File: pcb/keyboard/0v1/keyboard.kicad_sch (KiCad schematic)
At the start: 1 part, among them U1 113990583

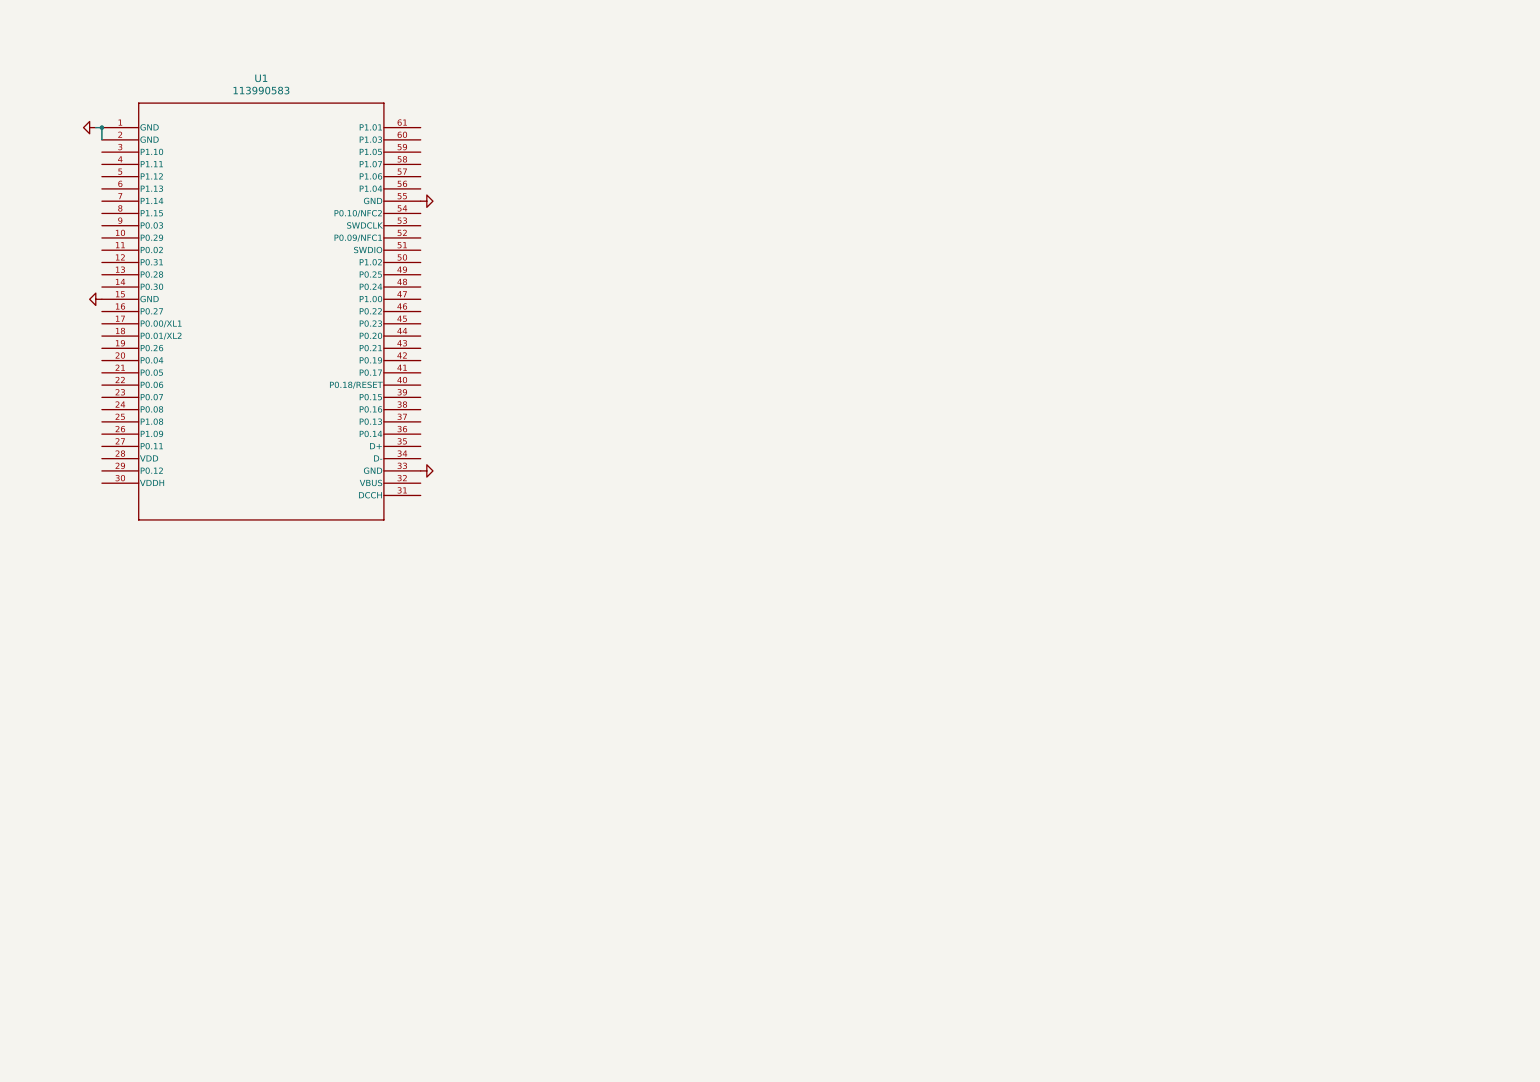
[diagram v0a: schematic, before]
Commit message: Basic power management circuit for the nrf52840 module.
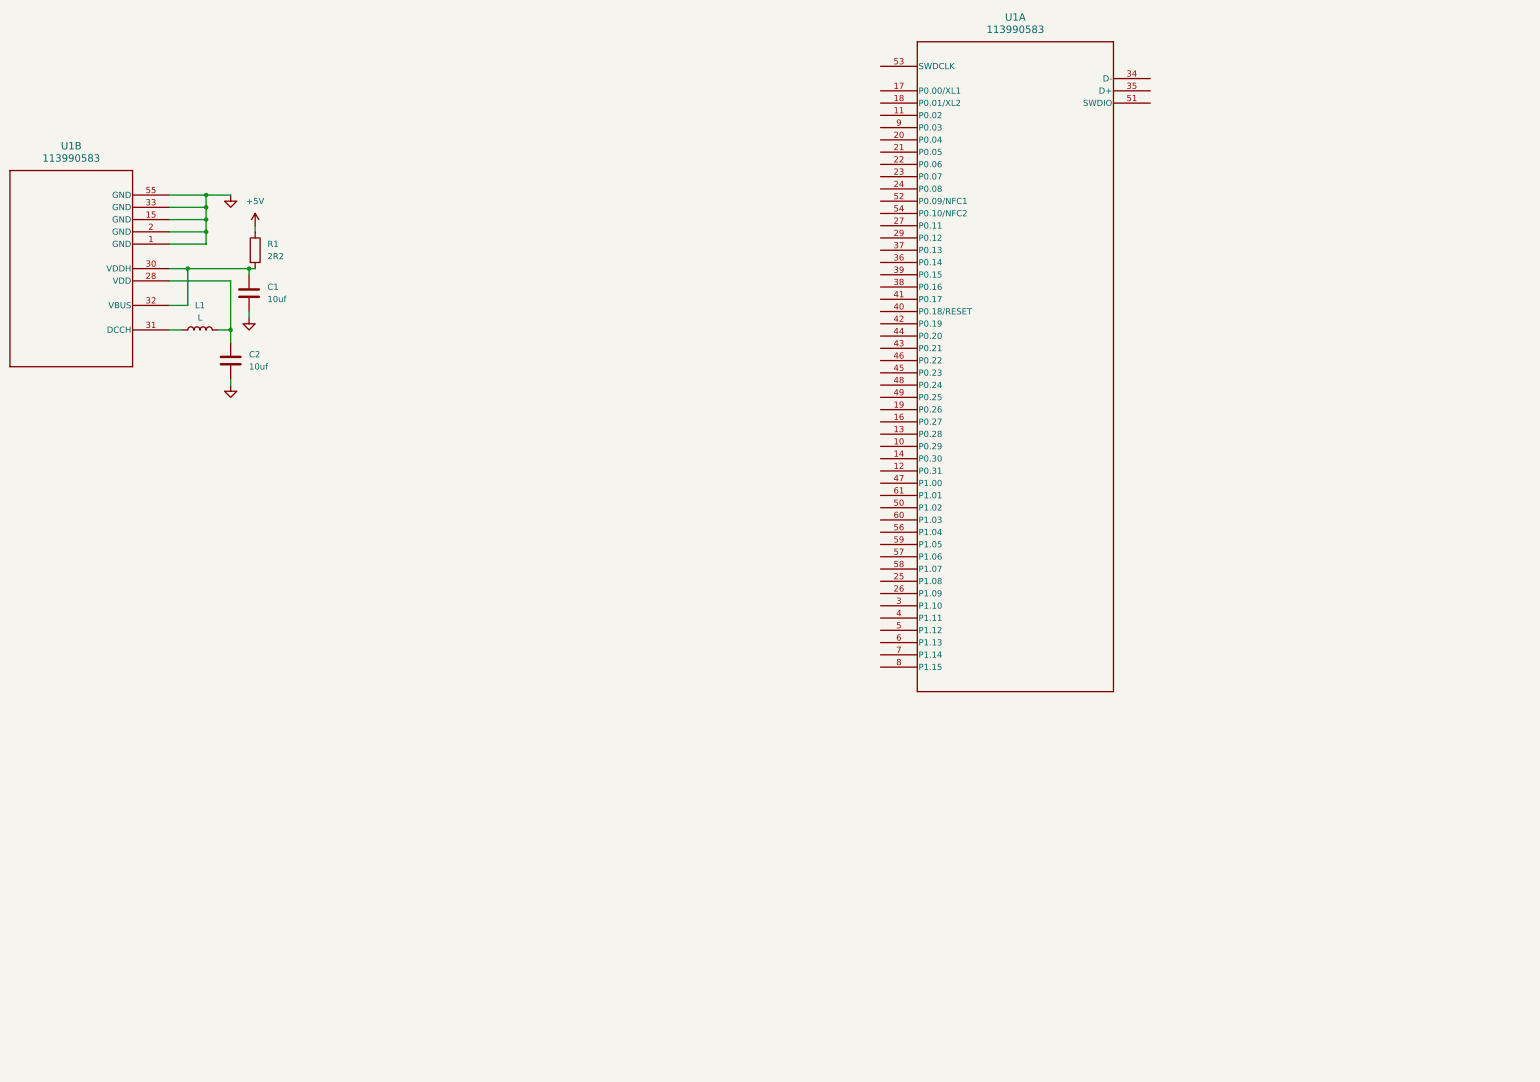
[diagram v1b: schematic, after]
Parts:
- added C1, C2: 10uf, Capacitor_SMD:C_0805_2012Metric, symbol Device:C
- added L1: L, Inductor_SMD:L_0603_1608Metric, symbol Device:L
- added R1: 2R2, Resistor_SMD:R_0603_1608Metric, symbol Device:R
- added unit 2 of U1
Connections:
- net GND: now also C1.2, C2.2, U1.1 (GND), U1.15 (GND), U1.2 (GND), U1.33 (GND), U1.55 (GND); no longer U1.1 (GND), U1.15 (GND), U1.2 (GND), U1.33 (GND), U1.55 (GND)
- new net: C2.1, L1.2, U1.28 (VDD)
- new net: C1.1, R1.2, U1.30 (VDDH), U1.32 (VBUS)
- new net: L1.1, U1.31 (DCCH)
- new net +5V: R1.1
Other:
- company: (none) -> Teahaz
- title: (none) -> TH-A10C keyboard

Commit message: Add USB and SWD Pogo connectors.
These are custom symbols, the footprint for them is yet to be added.
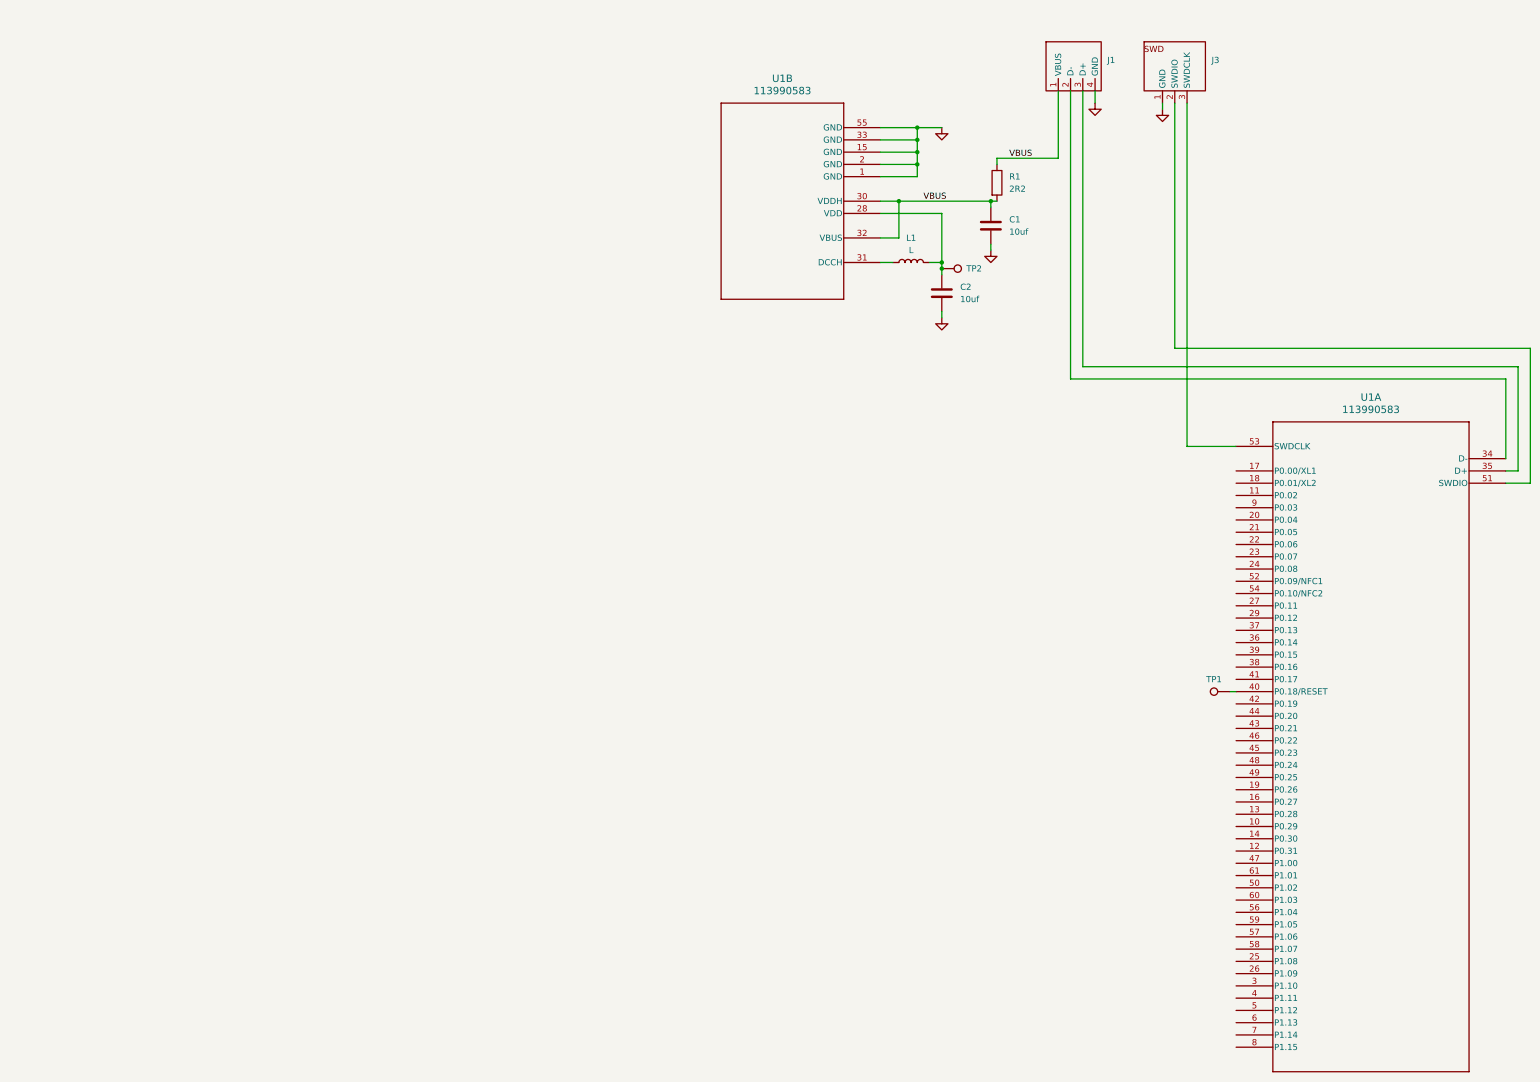
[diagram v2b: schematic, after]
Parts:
- added J1: ~, symbol TH-A10C:USB2_POGO_4
- added J3: ~, symbol TH-A10C:SWD_POGO_3
- added TP1, TP2: TestPoint, TestPoint:TestPoint_Pad_D2.0mm, symbol Connector:TestPoint
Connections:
- net +5V is gone; now on net VBUS: R1.1
- net GND: now also J1.4 (GND), J3.1 (GND)
- net at C2.1, L1.2, U1.28 (VDD): now also TP2.1
- net VBUS: now reaches C1.1, R1.2, U1.30 (VDDH), U1.32 (VBUS)
- net VBUS: now also J1.1 (VBUS)
- net at U1.34 (D-): now also J1.2 (D-)
- net at U1.35 (D+): now also J1.3 (D+)
- net at U1.40 (P0.18/RESET): now also TP1.1
- net at U1.51 (SWDIO): now also J3.2 (SWDIO)
- net at U1.53 (SWDCLK): now also J3.3 (SWDCLK)
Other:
- moved on the sheet: C1, C2, L1, R1, U1A, U1B
